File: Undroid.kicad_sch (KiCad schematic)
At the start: 26 parts, among them J1 AudioJack2, U1 ATSAME70J19A-AN

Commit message: main: New NorthBridge zone, include AllWinner A13 as ARM CPU.
Signed-off-by: Amlal EL Mahrouss <amlal@softwarelabs.com>
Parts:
- removed UR1: ESP-PSRAM32, Package_SO:SOIC-8_3.9x4.9mm_P1.27mm, symbol Memory_RAM:ESP-PSRAM32
- added R17, R18, R19, R20, R21: R, Resistor_SMD:R_0201_0603Metric, symbol Device:R
- added U2: AS4C256M16D3, Package_BGA:BGA-96_9.0x13.0mm_Layout2x3x16_P0.8mm, symbol Memory_RAM:AS4C256M16D3
- added U3: Allwinner-A13, Allwinner-A13:QFP40P2200X2200X160-177N, symbol Allwinner:Allwinner-A13
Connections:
- net CMD_F1: now also U1.56 (PD2); no longer U1.55 (PD3)
- net CMD_F2: now also U1.55 (PD3); no longer U1.54 (PD4)
- net GND: now also R19.2, R21.2; no longer U1.25 (PD22), U1.26 (PD21), U1.41 (PD12), U1.43 (PD11), U1.44 (PD10), U1.48 (PD9), U1.49 (PD8), U1.50 (PD7), U1.51 (PD6)
- net GSM_PWR_MOD: no longer U1.53 (PD5)
- net GSM_RST_MOD: no longer U1.36 (NRST), U1.57 (PD1)
- net SD_CMD: now also U1.57 (PD1); no longer U1.56 (PD2)
- net at U1.22 (PD24): now also U2.R3 (A9)
- net at U1.21 (PD26): now also U2.R7 (A11)
- net at U1.20 (PD25): now also U2.L7 (A10/AP)
- net at U1.2 (PD31): now also U2.N7 (A12/~{BC})
- net CPU_TST_MOD renamed PWR_TST
- new net: U3.100 (VCC), U3.142 (VCC), U3.163 (VCC), U3.5 (VCC)
- new net: U3.109 (VDD_INT), U3.149 (VDD_INT), U3.35 (VDD_INT), U3.73 (VDD_INT), U3.98 (VDD_INT)
- new net: U3.11 (VDD_CPU), U3.156 (VDD_CPU), U3.16 (VDD_CPU), U3.164 (VDD_CPU), U3.169 (VDD_CPU), U3.173 (VDD_CPU), U3.4 (VDD_CPU), U3.9 (VDD_CPU)
- new net: U2.H3 (DQ4), U3.19 (DDR3_D4)
- new net: U2.G2 (DQ6), U3.20 (DDR3_D6)
- new net: U2.F2 (DQ2), U3.21 (DDR3_D2)
- new net: U2.E3 (DQ0), U3.22 (DDR3_D0)
- new net: U3.23 (VCC_DRAM), U3.30 (VCC_DRAM), U3.43 (VCC_DRAM), U3.53 (VCC_DRAM), U3.62 (VCC_DRAM)
- new net: U2.C2 (DQ11), U3.24 (DDR3_D11)
- new net: U2.C3 (DQ9), U3.25 (DDR3_D9)
- new net: U2.A2 (DQ13), U3.26 (DDR3_D13)
- new net: U2.A3 (DQ15), U3.27 (DDR3_D15)
- new net: U2.A7 (DQ12), U3.36 (DDR3_D12)
- new net: U2.D7 (DQ8), U3.37 (DDR3_D8)
- new net: U2.B8 (DQ14), U3.38 (DDR3_D14)
- new net: U2.C8 (DQ10), U3.39 (DDR3_D10)
- new net: U2.F7 (DQ1), U3.40 (DDR3_D1)
- new net: U2.F8 (DQ3), U3.41 (DDR3_D3)
- new net: U2.H7 (DQ7), U3.42 (DDR3_D7)
- new net: U2.H8 (DQ5), U3.44 (DDR3_D5)
- new net: R18.2, U2.A1 (VDDQ), U2.A8 (VDDQ), U2.C1 (VDDQ), U2.C9 (VDDQ), U2.D2 (VDDQ), U2.E9 (VDDQ), U2.F1 (VDDQ), U2.H2 (VDDQ), U2.H9 (VDDQ)
- new net: R19.1, U2.A9 (VSS), U2.B3 (VSS), U2.E1 (VSS), U2.G8 (VSS), U2.J2 (VSS), U2.J8 (VSS), U2.M1 (VSS), U2.M9 (VSS), U2.P1 (VSS), U2.P9 (VSS), U2.T1 (VSS), U2.T9 (VSS)
- new net: R20.1, U2.B1 (VSSQ), U2.B9 (VSSQ), U2.D1 (VSSQ), U2.D8 (VSSQ), U2.E2 (VSSQ), U2.E8 (VSSQ), U2.F9 (VSSQ), U2.G1 (VSSQ), U2.G9 (VSSQ)
- new net: U1.25 (PD22), U2.T8 (A8)
- new net: U1.26 (PD21), U2.R2 (A7)
- new net: U1.41 (PD12), U2.R8 (A6)
- new net: U1.43 (PD11), U2.P2 (A5)
- new net: U1.44 (PD10), U2.P8 (A4)
- new net: U1.48 (PD9), U2.N2 (A3)
- new net: U1.49 (PD8), U2.P3 (A2)
- new net: U1.50 (PD7), U2.P7 (A1)
- new net: U1.51 (PD6), U2.N3 (A0)
- new net: U1.53 (PD5), U2.T3 (A13)
- new net: U1.54 (PD4), U2.T7 (A14)
- new net: R17.2, U2.B2 (VDD), U2.D9 (VDD), U2.G7 (VDD), U2.K2 (VDD), U2.K8 (VDD), U2.N1 (VDD), U2.N9 (VDD), U2.R1 (VDD), U2.R9 (VDD)
- new net LDM_RAM: U2.E7 (LDM)
- new net PWR_RESET: U1.36 (NRST), U2.T2 (~{RESET})
- new net PWR_RESET_N: U3.159 (RESET_N)
- new net RAM_CAS_N: U2.K3 (~{CAS})
- new net RAM_CK: U2.J7 (CK)
- new net RAM_CKE: U2.K9 (CKE)
- new net RAM_CK_N: U2.K7 (~{CK})
- new net RAM_CS_N: U2.L2 (~{CS})
- new net RAM_ODT: U2.K1 (ODT)
- new net RAM_RAS_N: U2.J3 (~{RAS})
- new net RAM_WE_N: U2.L3 (~{WE})
- new net UDM_RAM: U2.D3 (UDM)
- new net VDD: R17.1
- new net VDDQ: R18.1
- new net VSSQ: R20.2
- new net ZQ: U2.L8 (ZQ), U3.17 (DZQ)
- no-connect marks 9 -> 16
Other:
- moved on the sheet: AE1, FLASH1, FLASH2, G1, J1, PC1, R1, R10, R11, R12, R13, R14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

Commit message: main: update and fix schematic.
Signed-off-by: Amlal EL Mahrouss <amlal@softwarelabs.com>
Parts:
- added R22, R23, R24, R25: R, Resistor_SMD:R_0201_0603Metric, symbol Device:R
- added U4: USR-C322, RF_WiFi:USR-C322, symbol RF_WiFi:USR-C322
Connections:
- net +3.3V: now also R6.2, R8.2; no longer R6.1, R7.1, R8.1
- net GND: now also R18.1, R5.2, U1.45 (JTAGSEL), U1.5 (VREFP), U1.59 (DM), U1.60 (DP), R24.1, R25.2; no longer J1.S, R19.2, SD1.9 (SHIELD), U1.14 (GND), U1.31 (GND), U1.6 (GND)
- net VDDQ: now also R19.1; no longer R18.1
- net at U3.19 (DDR3_D4): no longer U2.H3 (DQ4)
- net at U3.20 (DDR3_D6): no longer U2.G2 (DQ6)
- net at U3.21 (DDR3_D2): no longer U2.F2 (DQ2)
- net at U3.22 (DDR3_D0): no longer U2.E3 (DQ0)
- net at U3.24 (DDR3_D11): no longer U2.C2 (DQ11)
- net at U3.25 (DDR3_D9): no longer U2.C3 (DQ9)
- net at U3.26 (DDR3_D13): no longer U2.A2 (DQ13)
- net at U3.27 (DDR3_D15): no longer U2.A3 (DQ15)
- net at U3.36 (DDR3_D12): no longer U2.A7 (DQ12)
- net at U3.37 (DDR3_D8): no longer U2.D7 (DQ8)
- net at U3.38 (DDR3_D14): no longer U2.B8 (DQ14)
- net at U3.39 (DDR3_D10): no longer U2.C8 (DQ10)
- net at U3.40 (DDR3_D1): no longer U2.F7 (DQ1)
- net at U3.41 (DDR3_D3): no longer U2.F8 (DQ3)
- net at U3.42 (DDR3_D7): no longer U2.H7 (DQ7)
- net at U3.44 (DDR3_D5): no longer U2.H8 (DQ5)
- net A10/AP: now reaches U3.48 (DDR3_A10)
- net A10/AP: now also U1.25 (PD22), U2.L7 (A10/AP)
- net A12/BC_N: now reaches U3.50 (DDR3_A12)
- net A12/BC_N: now also U1.20 (PD25), U2.N7 (A12/~{BC})
- net A4: now reaches U3.51 (DDR3_A4)
- net A4: now also U1.49 (PD8), U2.P8 (A4)
- net A1: now reaches U3.52 (DDR3_A1)
- net A1: now also U1.53 (PD5), U2.P7 (A1)
- net A6: now reaches U3.54 (DDR3_A6)
- net A6: now also U1.44 (PD10), U2.R8 (A6)
- net A8: now reaches U3.55 (DDR3_A8)
- net A8: now also U1.41 (PD12), U2.T8 (A8)
- net A11: now reaches U3.56 (DDR3_A11)
- net A11: now also U1.22 (PD24), U2.R7 (A11)
- net A14: now reaches U3.57 (DDR3_A14)
- net A14: now also U1.2 (PD31), U2.T7 (A14)
- net A0: now reaches U3.64 (DDR3_A0)
- net A0: now also U1.54 (PD4), U2.N3 (A0)
- net A3: now reaches U3.65 (DDR3_A3)
- net A3: now also U1.50 (PD7), U2.N2 (A3)
- net A2: now reaches U3.66 (DDR3_A2)
- net A2: now also U1.51 (PD6), U2.P3 (A2)
- net A5: now reaches U3.67 (DDR3_A5)
- net A5: now also U1.48 (PD9), U2.P2 (A5)
- net A13: now reaches U3.68 (DDR3_A13)
- net A13: now also U1.21 (PD26), U2.T3 (A13)
- net A9: now reaches U3.69 (DDR3_A9)
- net A9: now also U1.26 (PD21), U2.R3 (A9)
- net A7: now reaches U3.71 (DDR3_A7)
- net A7: now also U1.43 (PD11), U2.R2 (A7)
- net at FLASH1.4 (VSS), R9.1: no longer R5.2
- net at G1.9 (VDD_3V3): now also R6.1; no longer R6.2
- net at U2.A1 (VDDQ), U2.A8 (VDDQ), U2.C1 (VDDQ)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: now also R19.2; no longer R18.2
- net at R21.1: now also U1.14 (GND), U1.31 (GND), U1.6 (GND)
- net at G1.40 (VDD_EXT): now also R7.1; no longer R7.2
- net at U2.A9 (VSS), U2.B3 (VSS), U2.E1 (VSS)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: now also R18.2; no longer R19.1
- net RAM_UDQS_N: now reaches U2.B7 (~{UDQS})
- net RAM_UDQS: now reaches U2.C7 (UDQS)
- net RAM_LDQS: now reaches U2.F3 (LDQS)
- net RAM_LDQS_N: now reaches U2.G3 (~{LDQS})
- net at U2.H1 (VREFDQ): now also R22.2
- net RAM_BA0: now reaches U2.M2 (BA0)
- net RAM_BA2: now reaches U2.M3 (BA2)
- net at U2.M8 (VREFCA): now also R23.2
- net RAM_BA1: now reaches U2.N8 (BA1)
- net at G1.34 (VBAT), G1.35 (VBAT): now also R8.1; no longer R8.2
- new net: U4.1 (GND), U4.11 (GND), U4.12 (GND), U4.17 (GND), U4.28 (GND), U4.29 (GND), U4.44 (GND)
- new net: R24.2, SD1.9 (SHIELD)
- new net: J1.S, R25.1
- new net +1.8V: R7.2
- new net DQ00: U2.E3 (DQ0)
- new net DQ01: U2.F7 (DQ1)
- new net DQ02: U2.F2 (DQ2)
- new net DQ03: U2.F8 (DQ3)
- new net DQ04: U2.H3 (DQ4)
- new net DQ05: U2.H8 (DQ5)
- new net DQ06: U2.G2 (DQ6)
- new net DQ07: U2.H7 (DQ7)
- new net DQ08: U2.D7 (DQ8)
- new net DQ09: U2.C3 (DQ9)
- new net DQ10: U2.C8 (DQ10)
- new net DQ11: U2.C2 (DQ11)
- new net DQ12: U2.A7 (DQ12)
- new net DQ13: U2.A2 (DQ13)
- new net DQ14: U2.B8 (DQ14)
- new net DQ15: U2.A3 (DQ15)
- new net RAM_CA_REF: R23.1
- new net RAM_DQ_REF: R22.1
- no-connect marks 16 -> 9
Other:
- moved on the sheet: AE1, FLASH1, FLASH2, G1, J1, PC1, R1, R10, R11, R12, R13, R14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

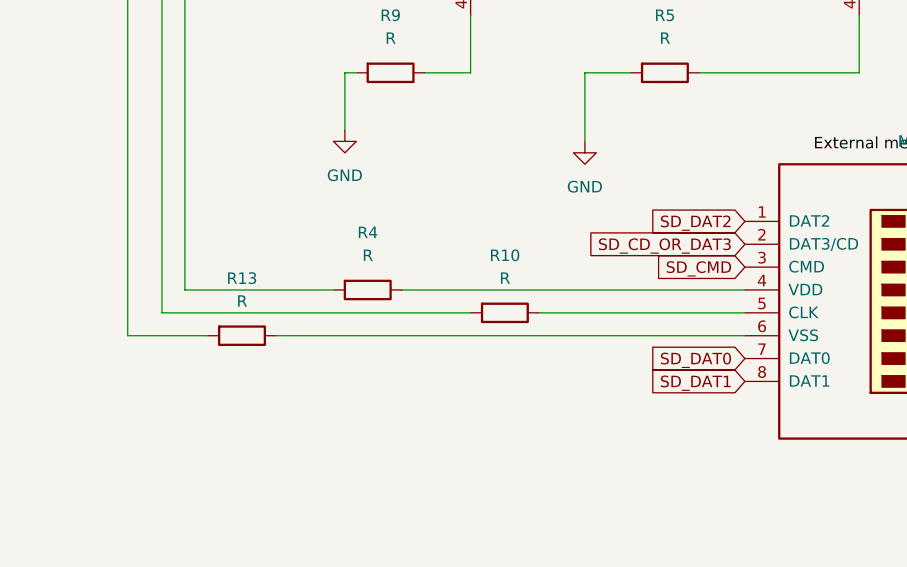
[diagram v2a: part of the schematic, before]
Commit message: main: remove useless 10K ohm resistor for CLK.
Signed-off-by: Amlal EL Mahrouss <amlal@softwarelabs.com>
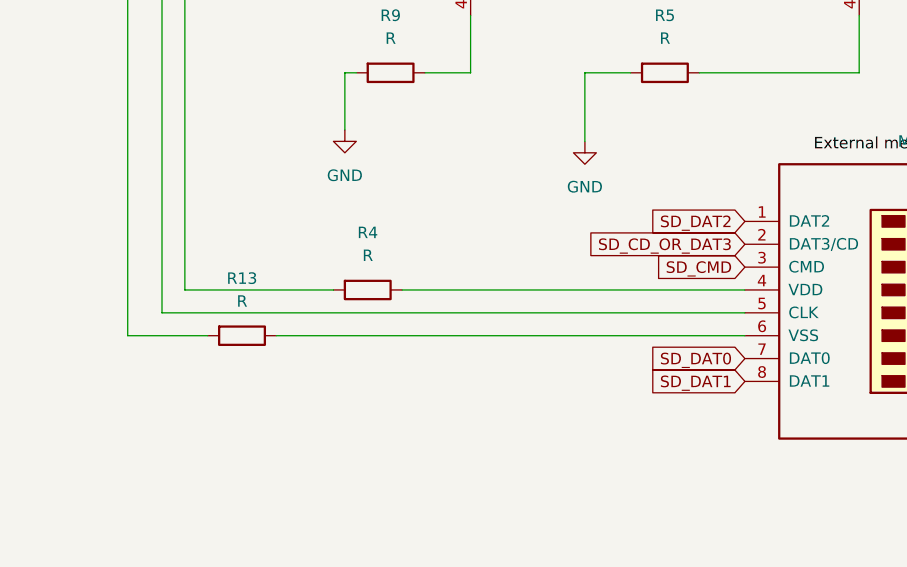
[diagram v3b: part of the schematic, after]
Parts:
- removed R10: R, Resistor_SMD:R_0201_0603Metric, symbol Device:R
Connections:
- net +3.3V: now also SD1.5 (CLK)
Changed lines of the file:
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@@
 	(wire
 		(pts
-			(xy 133.35 289.56) (xy 156.21 289.56)
-		)
-		(stroke
-			(width 0)
-			(type default)
-		)
-	)
-	(wire
-		(pts
 			(xy 368.3 364.49) (xy 367.03 364.49)
 		)
@@
 	(wire
 		(pts
-			(xy 91.44 289.56) (xy 125.73 289.56)
+			(xy 91.44 289.56) (xy 156.21 289.56)
 		)
 		(stroke
@@
 					(unit 1)
 				)
-			)
-		)
-	)
-	(symbol
-		(lib_id "Device:R")
-		(at 129.54 289.56 270)
-		(unit 1)
-		(exclude_from_sim no)
-		(in_bom yes)
-		(on_board yes)
-		(dnp no)
-		(fields_autoplaced yes)
-		(property "Reference" "R10"
-			(at 129.54 283.21 90)
-			(effects
-				(font
-					(size 1.27 1.27)
-				)
-			)
-		)
-		(property "Value" "R"
-			(at 129.54 285.75 90)
-			(effects
-				(font
-					(size 1.27 1.27)
-				)
-			)
-		)
-		(property "Footprint" "Resistor_SMD:R_0201_0603Metric"
-			(at 129.54 287.782 90)
-			(effects
-				(font
-					(size 1.27 1.27)
-				)
-				(hide yes)
-			)
-		)
-		(property "Datasheet" "~"
-			(at 129.54 289.56 0)
-			(effects
-				(font
-					(size 1.27 1.27)
-				)
-				(hide yes)
-			)
-		)
-		(property "Description" "Resistor"
-			(at 129.54 289.56 0)
-			(effects
-				(font
-					(size 1.27 1.27)
-				)
-				(hide yes)
-			)
-		)
-		(pin "1"
-		)
-		(pin "2"
-		)
-		(instances
-			(project "Undroid"
-				(path "/5d3a3bfa-72d2-42b8-bac3-6ac6fe44d852"
-					(reference "R10")
-					(unit 1)
-				)

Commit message: main: Update netlist.
Signed-off-by: Amlal EL Mahrouss <amlal@softwarelabs.com>
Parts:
- removed S1: SIM_Card, Connector_JAE:JAE_SIM_Card_SF72S006, symbol Connector:SIM_Card
- added J2: JAE_SIM_Card_SF72S006, Connector_JAE:JAE_SIM_Card_SF72S006, symbol Connector:JAE_SIM_Card_SF72S006
- SD1: footprint Connector_Card:SD-SIM_microSD-microSIM_Molex_104168-1620 -> Connector_Card:microSD_HC_Molex_104031-0811
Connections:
- net +3.3V: now also J2.C1 (VCC); no longer SD1.5 (CLK)
- net DQ00: now also U3.22 (DDR3_D0)
- net DQ01: now also U3.40 (DDR3_D1)
- net DQ02: now also U3.21 (DDR3_D2)
- net DQ03: now also U3.41 (DDR3_D3)
- net DQ04: now also U3.19 (DDR3_D4)
- net DQ05: now also U3.44 (DDR3_D5)
- net DQ06: now also U3.20 (DDR3_D6)
- net DQ07: now also U3.42 (DDR3_D7)
- net DQ08: now also U3.37 (DDR3_D8)
- net DQ09: now also U3.25 (DDR3_D9)
- net DQ10: now also U3.39 (DDR3_D10)
- net DQ11: now also U3.24 (DDR3_D11)
- net DQ12: now also U3.36 (DDR3_D12)
- net DQ13: now also U3.26 (DDR3_D13)
- net DQ14: now also U3.38 (DDR3_D14)
- net DQ15: now also U3.27 (DDR3_D15)
- net GSM_CLK: now also SD1.5 (CLK), J2.C3 (CLK)
- net GSM_IO: now also J2.C7 (I/O)
- net GSM_RST: now also J2.C2 (RST)
- net GSM_VPP: now also J2.C6 (VPP/SWP)
- net at R14.1: now also J2.C5 (GND)
- new net GSM_CSW: J2.CSW
- new net GSM_DSW: J2.DSW
- new net GSM_SH: J2.SH
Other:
- moved on the sheet: R11, R4
